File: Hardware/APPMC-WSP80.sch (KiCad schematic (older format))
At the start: 83 parts, among them J1 + 30V max, J10 STLINK-V3, J101 ADC_C, J102 ADC_D, J14 VDD, J15 PWM, J16 ADC_B, J17 3.0V, J18 1.5V, J2 VOut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

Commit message: MPU list errata
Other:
- note added: "alternative, pin-compatible MPUs, min 64k flash, 44-IO:\nSTM32G031C8Tx/Ux\nSTM32G041C8Tx/Ux\nSTM32G051C8Tx/Ux\nSTM32G061C8Tx/Ux\nSTM32G071C8Tx/Ux\nSTM32G071CBTx/Ux (128K)\nSTM32G081CBTx/Ux (128K)\nSTM32G0B1CBTx/Ux (128K)\nSTM32G0B1CCTx/Ux (256K)\nSTM32G0B1CETx/Ux (512k)"
- note removed: "MPU requirements: min 64kB Flash and VBAT input -> STM32G0/STM32F4 series in 48pin package"
- note removed: "alternative, pin-compatible MPUs:\nSTM32G031F8Px/G8Ux\nSTM32G041F8Px/G8Ux\nSTM32G051F8Px/G8Ux\nSTM32G061F8Px/G8Ux\nSTM32G071G8Ux/GBUx\nSTM32G081GBUx"
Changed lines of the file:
@@
 	0    1    1    0
 $EndComp
-Text Notes 5250 600  0    50   ~ 0
-MPU requirements: min 64kB Flash and VBAT input -> STM32G0/STM32F4 series in 48pin package
 Wire Wire Line
 	4950 1800 5200 1800
@@
 Text Label 4950 2700 0    50   ~ 0
 PWM
-Text Notes 3600 1200 0    50   ~ 0
-alternative, pin-compatible MPUs:\nSTM32G031F8Px/G8Ux\nSTM32G041F8Px/G8Ux\nSTM32G051F8Px/G8Ux\nSTM32G061F8Px/G8Ux\nSTM32G071G8Ux/GBUx\nSTM32G081GBUx
+Text Notes 3600 1400 0    50   ~ 0
+alternative, pin-compatible MPUs, min 64k flash, 44-IO:\nSTM32G031C8Tx/Ux\nSTM32G041C8Tx/Ux\nSTM32G051C8Tx/Ux\nSTM32G061C8Tx/Ux\nSTM32G071C8Tx/Ux\nSTM32G071CBTx/Ux (128K)\nSTM32G081CBTx/Ux (128K)\nSTM32G0B1CBTx/Ux (128K)\nSTM32G0B1CCTx/Ux (256K)\nSTM32G0B1CETx/Ux (512k)
 $Comp
 L STM32G0B1CEUx:STM32G0B1CEUx U5

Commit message: values adjusted
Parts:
- R9: value 3.44k -> 3.4k
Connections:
- net labels added: 22-53Ω 21-450°C
- net labels removed: 22.65-53Ω 20-450°C (37.5 avg)
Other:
- note added: "-32.51/+37.67mV"
- note added: "0.511÷2.66V"
- note added: "1.5V"
- note added: "gain=1+(100k/Rg)=30.41"
- note removed: "+32.5/-37.7mV"
- note removed: "gain=1+(100k/Rg)=30.07"
- note removed: "~~0.5÷2.9V"
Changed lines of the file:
@@
 P 2650 7250
 F 0 "#TH1" V 2750 7200 50  0000 L CNN
-F 1 "22.65-53Ω 20-450°C (37.5 avg)" V 2500 6900 50  0000 L CNN
+F 1 "22-53Ω 21-450°C" V 2500 6900 50  0000 L CNN
 F 2 "" H 2650 7250 50  0001 C CNN
 F 3 "~" H 2650 7250 50  0001 C CNN
@@
 	1850 5550 2200 5550
 Text Notes 3700 6850 0    50   ~ 0
-gain=1+(100k/Rg)=30.07
+gain=1+(100k/Rg)=30.41
 Wire Wire Line
 	1750 7050 3150 7050
@@
 	1400 5550 1850 5550
 Text Notes 3700 6750 0    50   Italic 0
-+32.5/-37.7mV
+-32.51/+37.67mV
 Wire Wire Line
 	2450 7250 2450 6800
@@
 U 1 1 6240A578
 P 5900 6450
-F 0 "J20" H 5750 6600 50  0000 L CNN
+F 0 "J20" H 5800 6300 50  0000 L CNN
 F 1 "ADC_A" H 5700 6400 50  0000 L CNN
 F 2 "Custom:PinHeader_1x01_P1.27mm_Vertical" H 5900 6450 50  0001 C CNN
@@
 P 4300 6350
 F 0 "R9" V 4150 6350 50  0000 C CNN
-F 1 "3.44k" V 4400 6400 50  0000 C CNN
+F 1 "3.4k" V 4400 6400 50  0000 C CNN
 F 2 "Custom:R_0805_2012Metric_Pad1.20x1.40mm_HandSolder_Jump" H 4300 6350 50  0001 C CNN
 F 3 "~" H 4300 6350 50  0001 C CNN
@@
 $EndComp
 Text Notes 5350 6350 0    50   ~ 0
-~~0.5÷2.9V
-Text Notes 1950 6400 0    50   ~ 0
+0.511÷2.66V
+Text Notes 2050 6450 0    50   ~ 0
 3.0V
 Text Notes 2300 7600 0    50   ~ 0
@@
 Text Notes 8350 7650 0    65   ~ 13
 configured as WSP80 driver
+Text Notes 3600 6250 0    50   ~ 0
+1.5V
 $EndSCHEMATC

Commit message: docs update
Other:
- note added: "0.511÷2.65V"
- note removed: "0.511÷2.66V"
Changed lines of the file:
@@
 $EndComp
 Text Notes 5350 6350 0    50   ~ 0
-0.511÷2.66V
+0.511÷2.65V
 Text Notes 2050 6450 0    50   ~ 0
 3.0V

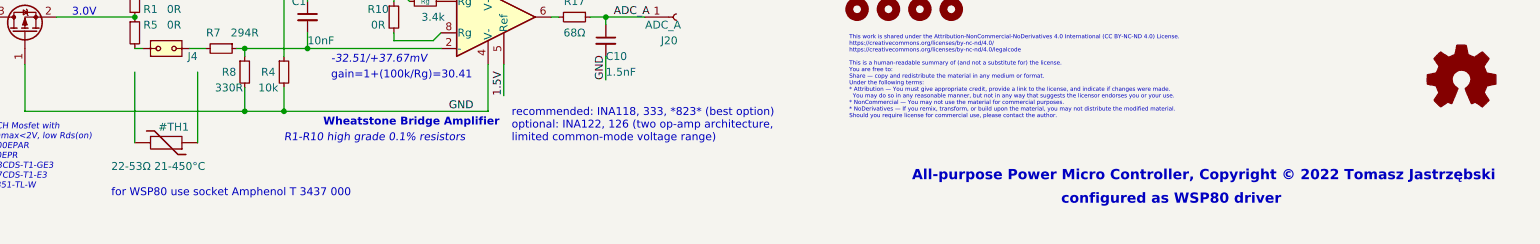
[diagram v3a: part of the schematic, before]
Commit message: docs & VS Code settings update
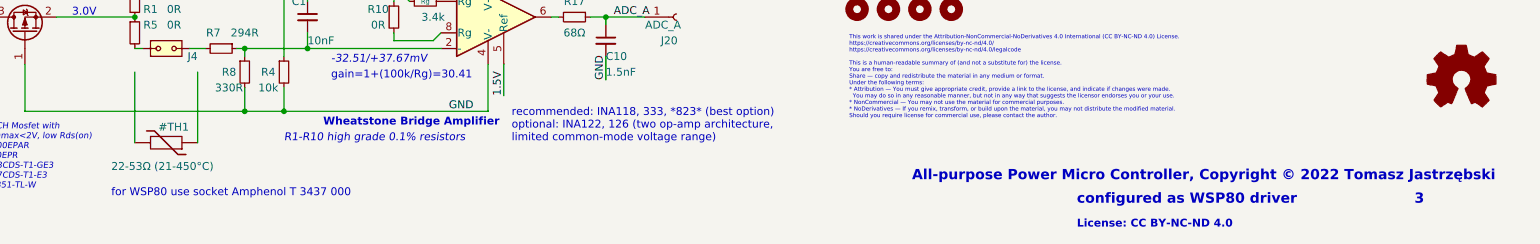
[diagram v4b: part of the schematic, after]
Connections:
- net labels added: 22-53Ω (21-450°C)
- net labels removed: 22-53Ω 21-450°C
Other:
- note added: "3"
- note added: "License: CC BY-NC-ND 4.0"
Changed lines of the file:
@@
 P 2650 7250
 F 0 "#TH1" V 2750 7200 50  0000 L CNN
-F 1 "22-53Ω 21-450°C" V 2500 6900 50  0000 L CNN
+F 1 "22-53Ω (21-450°C)" V 2500 6900 50  0000 L CNN
 F 2 "" H 2650 7250 50  0001 C CNN
 F 3 "~" H 2650 7250 50  0001 C CNN
@@
 Wire Wire Line
 	2750 6250 2900 6250
-Text Notes 8350 7650 0    65   ~ 13
+Text Notes 8450 7650 0    65   ~ 13
 configured as WSP80 driver
 Text Notes 3600 6250 0    50   ~ 0
 1.5V
+Text Notes 10600 7650 0    65   ~ 13
+3
+Text Notes 8450 7800 0    50   ~ 10
+License: CC BY-NC-ND 4.0
 $EndSCHEMATC

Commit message: updates to 3.1
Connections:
- net labels removed: WKUP
- wire segments 247 -> 246
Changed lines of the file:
@@
 Text Label 4900 1500 0    50   ~ 0
 ENC_B
-Text Label 6550 3200 0    50   ~ 0
+Text Label 4950 2900 0    50   ~ 0
 BTN
 Wire Wire Line
@@
 RX_B
 Wire Wire Line
-	6500 3200 6800 3200
-Wire Wire Line
 	5200 3800 4900 3800
 Wire Wire Line
@@
 Wire Wire Line
 	5200 2900 4900 2900
-Text Label 4950 2900 0    50   ~ 0
-WKUP
 Wire Wire Line
 	6500 2700 6800 2700

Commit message: update to 3.1
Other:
- note added: "3.1"
- note removed: "3"
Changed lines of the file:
@@
 1.5V
 Text Notes 10600 7650 0    65   ~ 13
-3
+3.1
 Text Notes 8450 7800 0    50   ~ 10
 License: CC BY-NC-ND 4.0

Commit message: update
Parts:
- U101: value OPA320 -> OPA388
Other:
- note added: "any low-offset (<0.1mV),\nhigh output current OpAmp\n*high CLoad drive*\nOPA388, NCS2005 (light capacitive load)\nOPA350EA (up to 1µF, MSOP-8 pkg)\nLM8261 (unlimited capacitive load use, lower precision)"
- note added: "for WSP80 use socket: Amphenol T 3437 000"
- note removed: "any low-offset (<0.1mV),\nhigh output current OpAmp"
- note removed: "for WSP80 use socket Amphenol T 3437 000"
- moved on the sheet: C1, C10, C101, C2, C24, C3, C4, C5, C6, C7, C8, D1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

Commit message: update
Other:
- note added: "any low-offset (<0.1mV),\nhigh output current OpAmp\n*high CLoad drive*\nOPA388, NCS2005 (light capacitive load)\nOPA350EA (up to 1µF, MSOP-8 pkg)\nLM8261 (unlimited capacitive load, lower precision)"
- note removed: "any low-offset (<0.1mV),\nhigh output current OpAmp\n*high CLoad drive*\nOPA388, NCS2005 (light capacitive load)\nOPA350EA (up to 1µF, MSOP-8 pkg)\nLM8261 (unlimited capacitive load use, lower precision)"
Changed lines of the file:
@@
 3.0V
 Text Notes 500  6950 0    50   Italic 0
-any low-offset (<0.1mV),\nhigh output current OpAmp\n*high CLoad drive*\nOPA388, NCS2005 (light capacitive load)\nOPA350EA (up to 1µF, MSOP-8 pkg)\nLM8261 (unlimited capacitive load use, lower precision)
+any low-offset (<0.1mV),\nhigh output current OpAmp\n*high CLoad drive*\nOPA388, NCS2005 (light capacitive load)\nOPA350EA (up to 1µF, MSOP-8 pkg)\nLM8261 (unlimited capacitive load, lower precision)
 $Comp
 L Device:C_Small C101
